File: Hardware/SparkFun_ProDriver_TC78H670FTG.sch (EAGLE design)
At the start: 49 parts, among them J1 POWER_JACKTOE, J2 LATCH, J3 PTH, J4 LATCH, J5 LATCH, J6 PTH, J7 LATCH, J8 PTH, U1 TC78H670FTG, U2 LM1117

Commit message: Added new jeep pro driver logo to bottom silk
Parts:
- added U$41: PRODRIVER_LOGO, TC78H670FTG:PRODRIVER_LOGO
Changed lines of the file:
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@@
 <?xml version="1.0" encoding="utf-8"?>
 <!DOCTYPE eagle SYSTEM "eagle.dtd">
-<eagle version="9.5.2">
+<eagle version="9.6.2">
 <drawing>
 <settings>
@@
 <part name="GND16" library="SparkFun-PowerSymbols" library_urn="urn:adsk.eagle:library:530" deviceset="GND" device=""/>
 <part name="GND11" library="SparkFun-PowerSymbols" deviceset="GND" device=""/>
+<part name="U$41" library="TC78H670FTG" deviceset="PRODRIVER_LOGO" device=""/>
 </parts>
 <sheets>
@@
 <instance part="FID1" gate="G$1" x="234.696" y="26.416" smashed="yes"/>
 <instance part="FID2" gate="G$1" x="234.696" y="31.496" smashed="yes"/>
-<instance part="LOGO1" gate="G$1" x="60.96" y="1.27" smashed="yes"/>
+<instance part="LOGO1" gate="G$1" x="40.64" y="1.27" smashed="yes"/>
 <instance part="LOGO2" gate="G$1" x="133.096" y="13.462" smashed="yes"/>
 <instance part="FRAME1" gate="G$1" x="0" y="0" smashed="yes"/>
@@
 <attribute name="VALUE" x="83.82" y="60.706" size="1.778" layer="96" font="vector" align="top-center"/>
 </instance>
+<instance part="U$41" gate="G$1" x="109.22" y="22.86" smashed="yes"/>
 </instances>
 <busses>

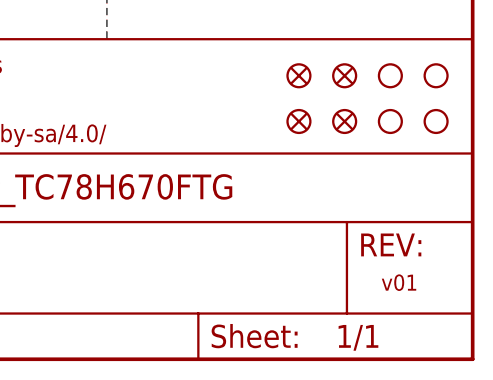
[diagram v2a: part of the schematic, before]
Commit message: Rotated bottom silk labels to match product name/logo
also updated version number to v10 in brd bottom copper and sch
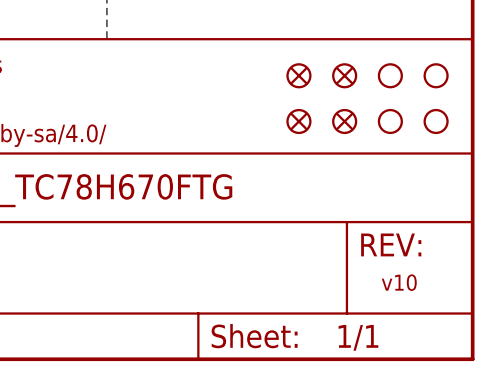
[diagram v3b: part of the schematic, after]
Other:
- note added: "v10"
- note removed: "v01"
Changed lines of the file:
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@@
 <sheet>
 <plain>
-<text x="238.76" y="7.62" size="1.778" layer="94" font="vector">v01</text>
+<text x="238.76" y="7.62" size="1.778" layer="94" font="vector">v10</text>
 <text x="170.688" y="11.43" size="2.54" layer="94" font="vector">Pete Lewis</text>
 <text x="2.54" y="180.34" size="2.54" layer="94" font="vector" ratio="14">Power Input</text>

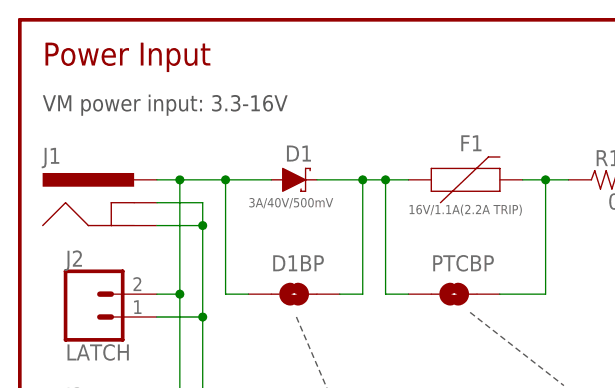
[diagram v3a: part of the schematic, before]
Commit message: Corrected input voltage range to 3.6-16V on sch and brd
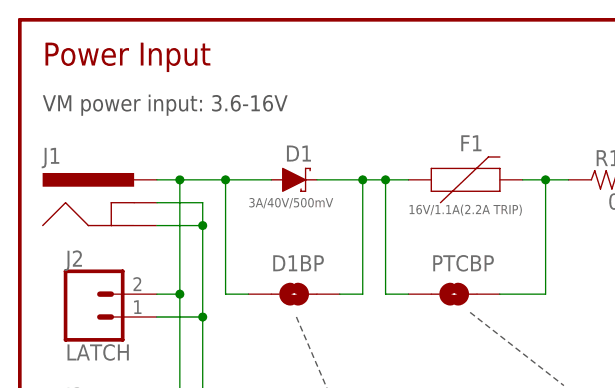
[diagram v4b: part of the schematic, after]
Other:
- note added: "VM power input: 3.6-16V"
- note removed: "VM power input: 3.3-16V"
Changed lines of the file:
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@@
 to disable LED</text>
 <wire x1="172.72" y1="185.42" x2="172.72" y2="124.46" width="0.2032" layer="97" style="longdash"/>
-<text x="2.54" y="175.26" size="1.778" layer="97" font="vector">VM power input: 3.3-16V</text>
+<text x="2.54" y="175.26" size="1.778" layer="97" font="vector">VM power input: 3.6-16V</text>
 <wire x1="248.92" y1="53.34" x2="208.28" y2="53.34" width="0.2032" layer="97" style="longdash"/>
 <text x="211.074" y="42.164" size="1.778" layer="94" font="vector" ratio="12">THIS IS A 4-LAYER BOARD</text>

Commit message: Replaced IC device to use sparkfun eagle library
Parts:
- U1: device TC78H670FTG:TC78H670FTG -> SparkFun-IC-Special-Function:TC78H670FTG
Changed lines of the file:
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@@
 <part name="J8" library="SparkFun-Connectors" deviceset="CONN_04" device="1X04_NO_SILK" value="PTH"/>
 <part name="J3" library="SparkFun-Connectors" deviceset="CONN_02" device="1X02_NO_SILK" value="PTH"/>
-<part name="U1" library="TC78H670FTG" deviceset="TC78H670FTG" device=""/>
+<part name="U1" library="SparkFun-IC-Special-Function" deviceset="TC78H670FTG" device="" value="TC78H670FTG"/>
 <part name="GND1" library="SparkFun-PowerSymbols" deviceset="GND" device=""/>
 <part name="GND2" library="SparkFun-PowerSymbols" deviceset="GND" device=""/>
